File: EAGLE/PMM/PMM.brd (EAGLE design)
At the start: 76.2 x 50.8 mm, 19 parts, among them J1 TB001-500-12BE, K1 EC2-5NU, K2 G6DN-1A_DC5, K3 35701331, K4 35701331

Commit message: Minor format fixes
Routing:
- net N$5: track 75.5 -> 72.5 mm
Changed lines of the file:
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@@
 <contactref element="K2" pad="1"/>
 <wire x1="69.85" y1="17.78" x2="67.31" y2="20.32" width="0.254" layer="16"/>
-<wire x1="67.31" y1="20.32" x2="33.02" y2="20.32" width="0.254" layer="16"/>
-<wire x1="33.02" y1="20.32" x2="24.13" y2="29.21" width="0.254" layer="16"/>
-<wire x1="24.13" y1="29.21" x2="24.13" y2="34.29" width="0.254" layer="16"/>
-<wire x1="24.13" y1="34.29" x2="13.97" y2="44.45" width="0.254" layer="16"/>
+<wire x1="67.31" y1="20.32" x2="38.1" y2="20.32" width="0.254" layer="16"/>
+<wire x1="38.1" y1="20.32" x2="13.97" y2="44.45" width="0.254" layer="16"/>
 <wire x1="13.97" y1="44.45" x2="10.16" y2="44.45" width="0.254" layer="16"/>
 <wire x1="10.16" y1="44.45" x2="8.89" y2="45.72" width="0.254" layer="16"/>

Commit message: Updated C4 value
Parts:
- C4: value 0.33uF -> 0.47uF
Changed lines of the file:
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@@
 <attribute name="VALUE" x="64.008" y="41.275" size="1.27" layer="27" ratio="10"/>
 </element>
-<element name="C4" library="capacitor-wima" library_urn="urn:adsk.eagle:library:116" package="C10B6" package3d_urn="urn:adsk.eagle:package:5401/1" value="0.33uF" x="31.75" y="38.1" smashed="yes" rot="R180">
+<element name="C4" library="capacitor-wima" library_urn="urn:adsk.eagle:library:116" package="C10B6" package3d_urn="urn:adsk.eagle:package:5401/1" value="0.47uF" x="31.75" y="38.1" smashed="yes" rot="R180">
 <attribute name="NAME" x="27.94" y="34.798" size="1.27" layer="25" ratio="10" rot="R180"/>
 <attribute name="POPULARITY" value="0" x="31.75" y="38.1" size="1.778" layer="27" rot="R180" display="off"/>

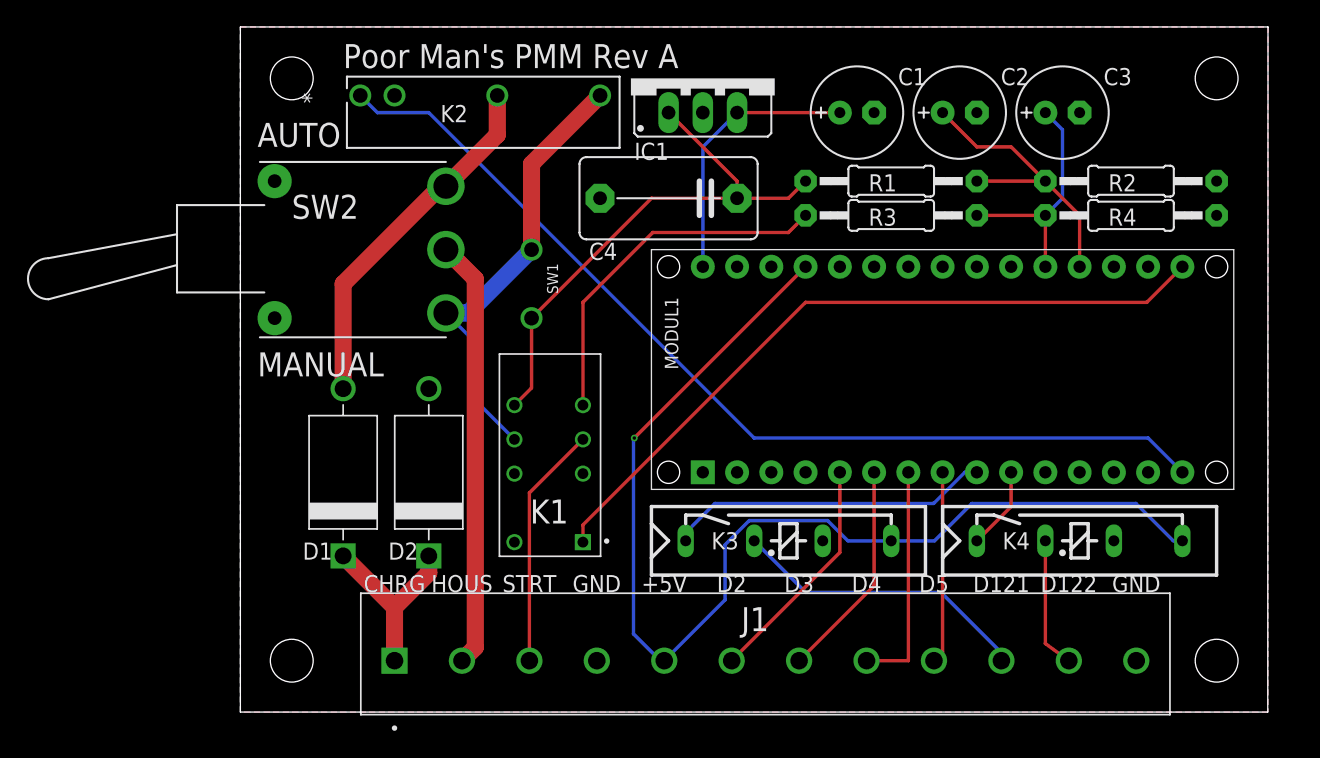
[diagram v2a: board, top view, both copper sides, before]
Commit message: Switched D12 & D13 to have on-board indicator for on state
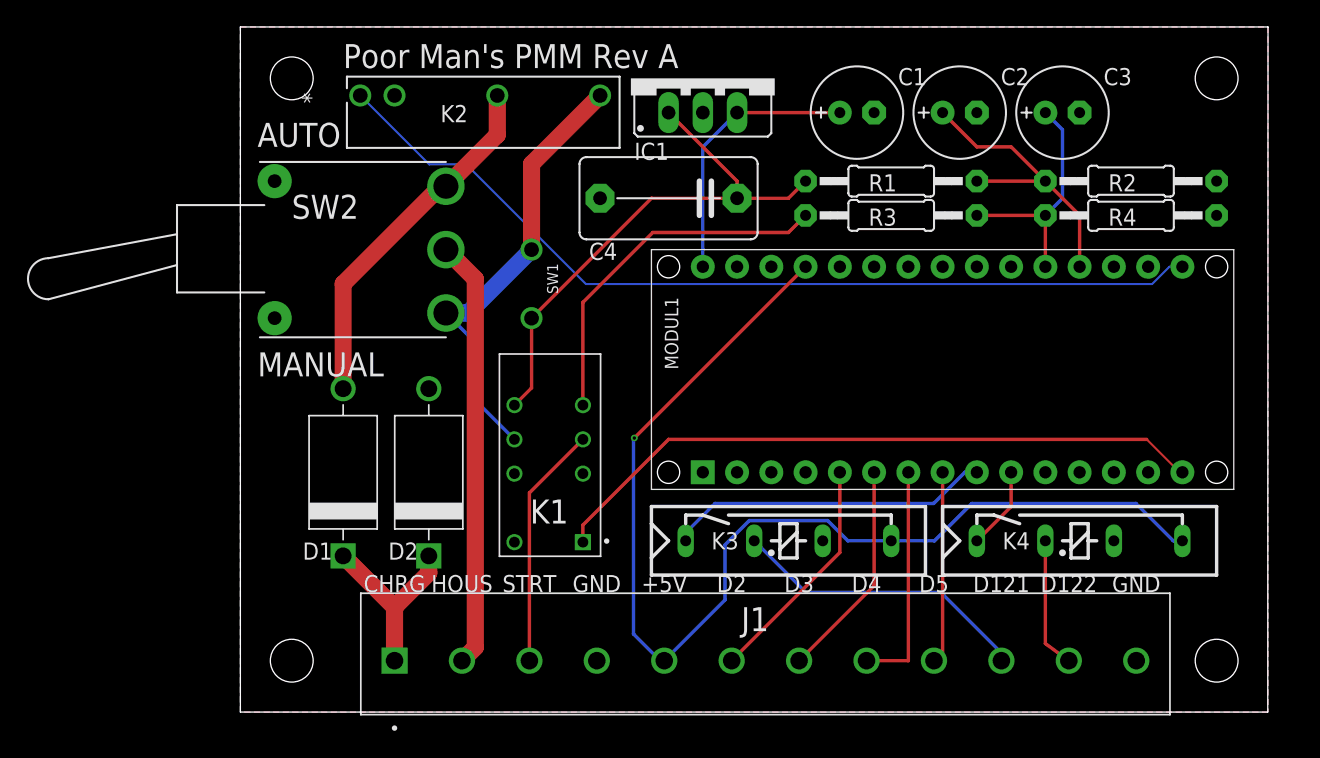
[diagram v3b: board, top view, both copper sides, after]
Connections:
- removed net N$6: K1.1, MODUL1.J2.15
- new net N$22: K1.1, MODUL1.J1.15
- net N$5: now also MODUL1.J2.15; no longer MODUL1.J1.15
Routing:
- net N$6: track 53.7 -> 0.00 mm
- net N$22: track 0.00 -> 49.4 mm
- net N$5: track 72.5 -> 67.3 mm
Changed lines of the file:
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@@
 <wire x1="30.48" y1="38.1" x2="36.83" y2="38.1" width="0.254" layer="1"/>
-</signal>
-<signal name="N$5">
-<contactref element="MODUL1" pad="J1.15"/>
-<contactref element="K2" pad="1"/>
-<wire x1="69.85" y1="17.78" x2="67.31" y2="20.32" width="0.254" layer="16"/>
-<wire x1="67.31" y1="20.32" x2="38.1" y2="20.32" width="0.254" layer="16"/>
-<wire x1="38.1" y1="20.32" x2="13.97" y2="44.45" width="0.254" layer="16"/>
-<wire x1="13.97" y1="44.45" x2="10.16" y2="44.45" width="0.254" layer="16"/>
-<wire x1="10.16" y1="44.45" x2="8.89" y2="45.72" width="0.254" layer="16"/>
-</signal>
-<signal name="N$6">
-<contactref element="MODUL1" pad="J2.15"/>
-<contactref element="K1" pad="1"/>
-<wire x1="69.85" y1="33.02" x2="67.21" y2="30.38" width="0.254" layer="1"/>
-<wire x1="67.21" y1="30.38" x2="41.91" y2="30.38" width="0.254" layer="1"/>
-<wire x1="41.91" y1="30.38" x2="25.4" y2="13.87" width="0.254" layer="1"/>
-<wire x1="25.4" y1="13.87" x2="25.4" y2="12.6" width="0.254" layer="1"/>
 </signal>
 <signal name="GND">
@@
 <wire x1="57.15" y1="15.24" x2="54.61" y2="12.7" width="0.254" layer="1"/>
 </signal>
+<signal name="N$22">
+<contactref element="MODUL1" pad="J1.15"/>
+<contactref element="K1" pad="1"/>
+<wire x1="67.21" y1="20.22" x2="31.75" y2="20.22" width="0.254" layer="1"/>
+<wire x1="31.75" y1="20.22" x2="25.4" y2="13.87" width="0.254" layer="1"/>
+<wire x1="25.4" y1="13.87" x2="25.4" y2="12.6" width="0.254" layer="1"/>
+<wire x1="69.85" y1="17.78" x2="69.65" y2="17.78" width="0.1524" layer="1"/>
+<wire x1="69.65" y1="17.78" x2="67.21" y2="20.22" width="0.1524" layer="1"/>
+</signal>
+<signal name="N$5">
+<contactref element="MODUL1" pad="J2.15"/>
+<contactref element="K2" pad="1"/>
+<wire x1="69.85" y1="33.02" x2="68.89053125" y2="33.02" width="0.1524" layer="16"/>
+<wire x1="14.00175" y1="40.60825" x2="8.89" y2="45.72" width="0.1524" layer="16"/>
+<wire x1="25.62444375" y1="31.7373" x2="16.75349375" y2="40.60825" width="0.1524" layer="16"/>
+<wire x1="16.75349375" y1="40.60825" x2="14.00175" y2="40.60825" width="0.1524" layer="16"/>
+<wire x1="68.89053125" y1="33.02" x2="67.60783125" y2="31.7373" width="0.1524" layer="16"/>
+<wire x1="67.60783125" y1="31.7373" x2="25.62444375" y2="31.7373" width="0.1524" layer="16"/>
+</signal>
 </signals>

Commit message: Corrected SW2 footprint
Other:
- board text added: "Poor Man's PMM Rev B"
- board text removed: "Poor Man's PMM Rev A"
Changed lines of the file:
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@@
 <hole x="72.39" y="46.99" drill="3.175"/>
 <hole x="72.39" y="3.81" drill="3.175"/>
-<text x="7.62" y="49.53" size="1.778" layer="21" align="top-left">Poor Man's PMM Rev A</text>
+<text x="7.62" y="49.53" size="1.778" layer="21" align="top-left">Poor Man's PMM Rev B</text>
 <text x="26.4287" y="8.89" size="1.27" layer="21" align="bottom-center">GND</text>
 <text x="21.42998125" y="8.89" size="1.27" layer="21" align="bottom-center">STRT</text>

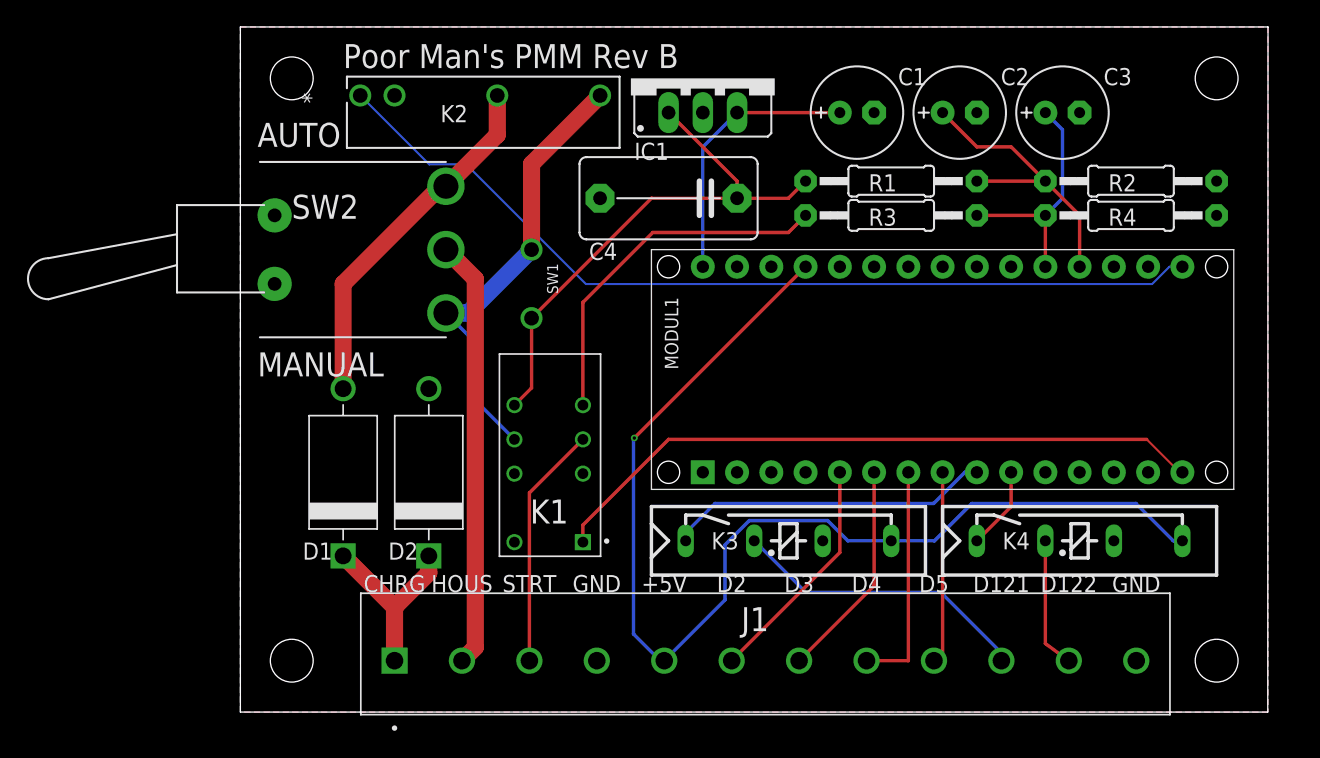
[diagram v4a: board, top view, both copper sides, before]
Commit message: Added indicator LEDs
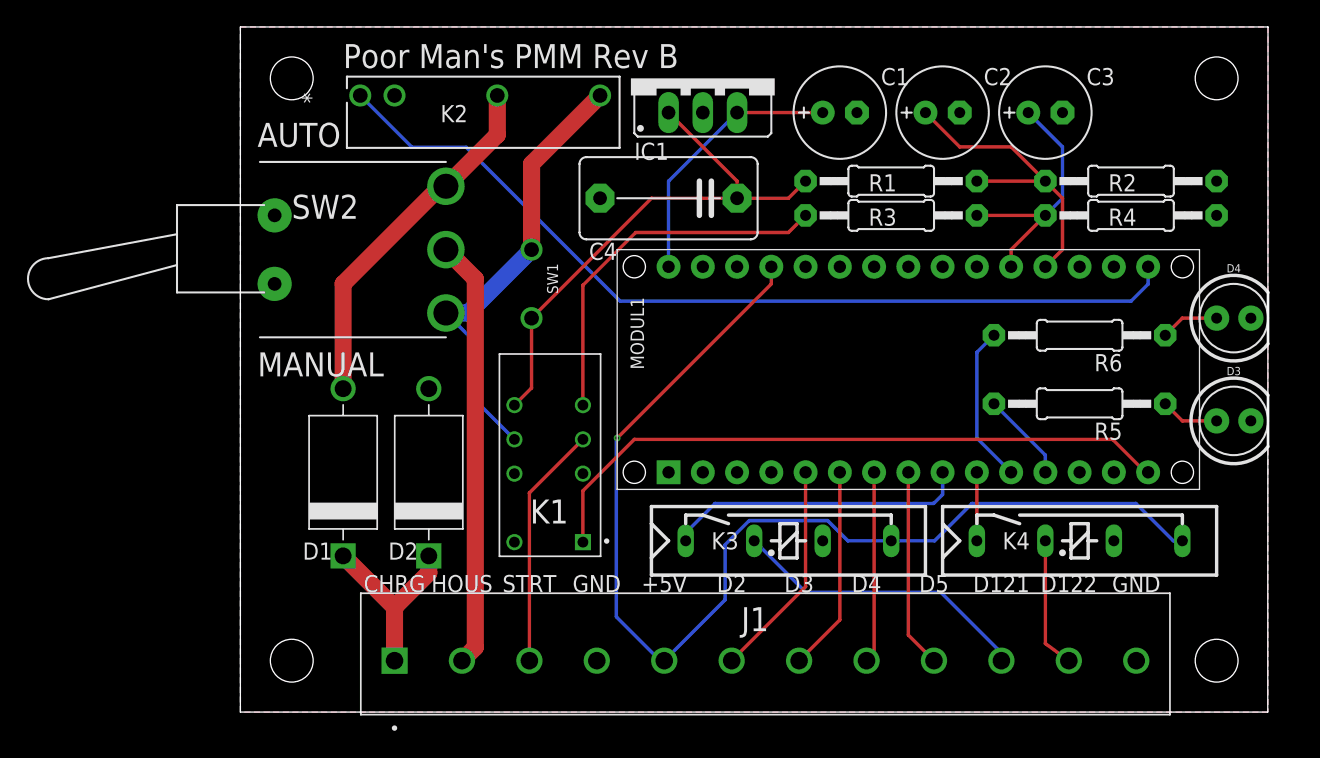
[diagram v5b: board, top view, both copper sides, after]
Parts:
- added D3: GRN, SparkFun-LED:LED_5MM-KIT
- added D4: YLW, SparkFun-LED:LED_5MM-KIT
- added R5, R6: 220, adafruit:0207/12
- moved MODUL1 2.54 mm to (49.5, 25.4)
- moved C2 1.27 mm to (52.1, 44.5)
- moved C3 1.27 mm to (59.7, 44.5)
- moved C1 1.27 mm to (44.5, 44.5)
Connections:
- new net N$23: D3.A, R5.1
- new net N$24: MODUL1.J1.11, R6.2
- new net N$25: MODUL1.J1.12, R5.2
- new net N$6: D4.A, R6.1
- net GND: now also D3.K, D4.K
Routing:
- net N$24: track 0.00 -> 11.7 mm
- net N$25: track 0.00 -> 6.66 mm
- net N$6: track 0.00 -> 4.34 mm
- net N$23: track 0.00 -> 4.34 mm
- net N$16: track 17.1 -> 14.5 mm
- net N$11: track 17.6 -> 19.1 mm
- net N$19: track 24.0 -> 22.5 mm
- net N$8: track 22.2 -> 23.5 mm
- net N$14: track 17.3 -> 16.2 mm
- net N$21: track 6.13 -> 5.08 mm
- net N$15: track 16.3 -> 15.2 mm
- net N$22: track 49.4 -> 48.3 mm
- net N$12: track 26.8 -> 27.5 mm
- net N$5: track 67.3 -> 66.5 mm
- net N$17: track 14.2 -> 14.8 mm

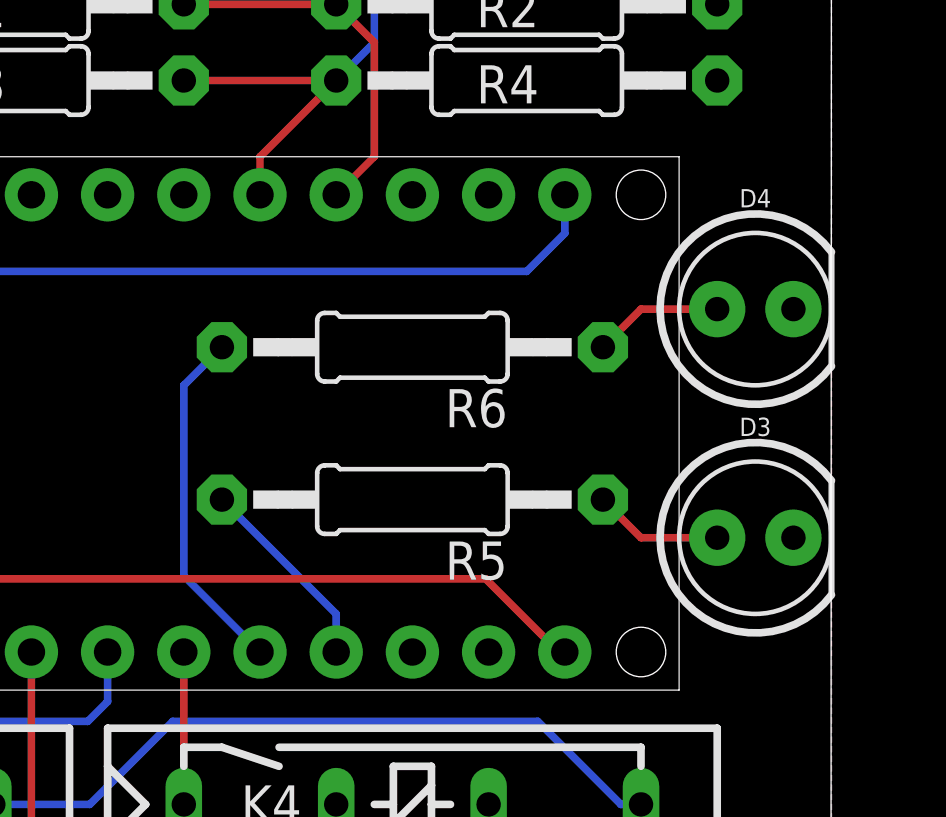
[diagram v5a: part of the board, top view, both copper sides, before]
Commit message: Rotated LEDs to bring pads in from board edge
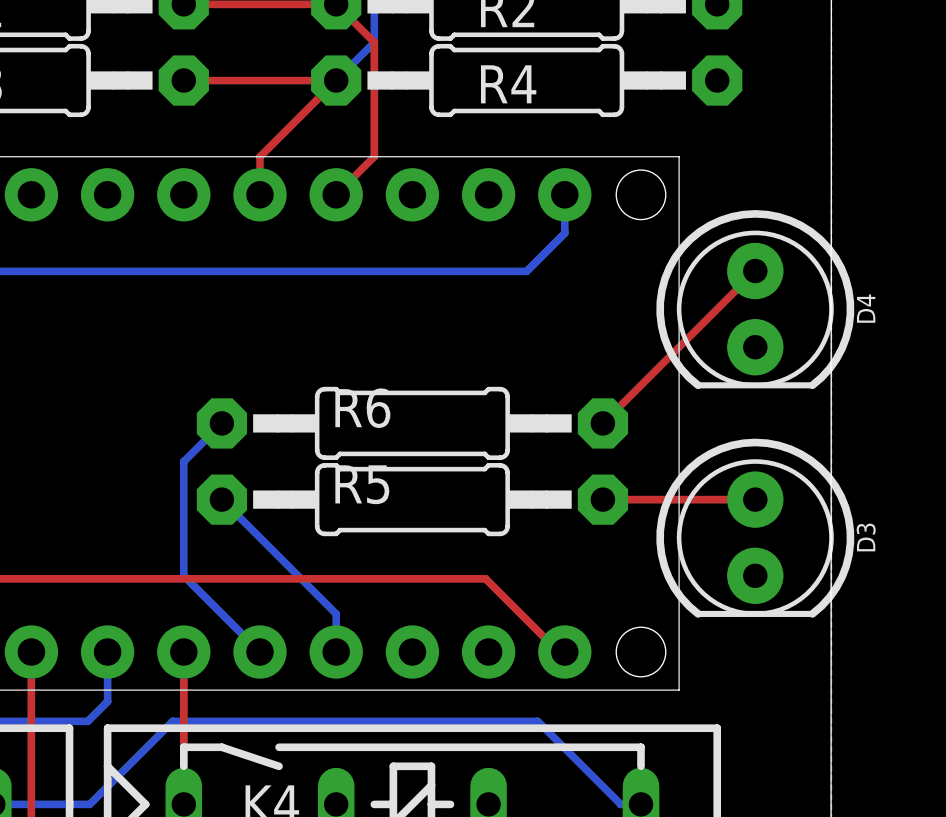
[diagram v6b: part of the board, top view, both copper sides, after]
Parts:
- moved R6 2.54 mm to (62.2, 25.4)
- turned D3 to 270 degrees
- turned D4 to 270 degrees
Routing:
- net N$6: track 4.34 -> 7.18 mm
- net N$24: track 11.7 -> 9.20 mm
- net N$23: track 4.34 -> 5.08 mm
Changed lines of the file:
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@@
 <attribute name="VALUE" x="59.69" y="15.875" size="1.27" layer="27"/>
 </element>
-<element name="D3" library="SparkFun-LED" package="LED_5MM-KIT" value="GRN" x="73.66" y="21.59" smashed="yes">
-<attribute name="NAME" x="73.66" y="24.9809" size="0.6096" layer="25" font="vector" ratio="20" align="bottom-center"/>
-<attribute name="VALUE" x="73.6854" y="18.1991" size="0.6096" layer="27" font="vector" ratio="20" align="top-center"/>
-</element>
-<element name="D4" library="SparkFun-LED" package="LED_5MM-KIT" value="YLW" x="73.66" y="29.21" smashed="yes">
-<attribute name="NAME" x="73.66" y="32.6009" size="0.6096" layer="25" font="vector" ratio="20" align="bottom-center"/>
-<attribute name="VALUE" x="73.6854" y="25.8191" size="0.6096" layer="27" font="vector" ratio="20" align="top-center"/>
+<element name="D3" library="SparkFun-LED" package="LED_5MM-KIT" value="GRN" x="73.66" y="21.59" smashed="yes" rot="R270">
+<attribute name="NAME" x="77.0509" y="21.59" size="0.6096" layer="25" font="vector" ratio="20" rot="R270" align="bottom-center"/>
+<attribute name="VALUE" x="70.2691" y="21.5646" size="0.6096" layer="27" font="vector" ratio="20" rot="R270" align="top-center"/>
+</element>
+<element name="D4" library="SparkFun-LED" package="LED_5MM-KIT" value="YLW" x="73.66" y="29.21" smashed="yes" rot="R270">
+<attribute name="NAME" x="77.0509" y="29.21" size="0.6096" layer="25" font="vector" ratio="20" rot="R270" align="bottom-center"/>
+<attribute name="VALUE" x="70.2691" y="29.1846" size="0.6096" layer="27" font="vector" ratio="20" rot="R270" align="top-center"/>
 </element>
 <element name="R5" library="adafruit" library_urn="urn:adsk.eagle:library:420" package="0207/12" package3d_urn="urn:adsk.eagle:package:6240598/1" value="220" x="62.23" y="22.86" smashed="yes" rot="R180">
-<attribute name="NAME" x="65.405" y="21.463" size="1.27" layer="25" ratio="10" rot="R180"/>
+<attribute name="NAME" x="61.595" y="24.003" size="1.27" layer="25" ratio="10" rot="R180"/>
 <attribute name="VALUE" x="64.516" y="23.5458" size="1.27" layer="27" ratio="10" rot="R180"/>
 </element>
-<element name="R6" library="adafruit" library_urn="urn:adsk.eagle:library:420" package="0207/12" package3d_urn="urn:adsk.eagle:package:6240598/1" value="220" x="62.23" y="27.94" smashed="yes" rot="R180">
-<attribute name="NAME" x="65.405" y="26.543" size="1.27" layer="25" ratio="10" rot="R180"/>
-<attribute name="VALUE" x="64.516" y="28.6258" size="1.27" layer="27" ratio="10" rot="R180"/>
+<element name="R6" library="adafruit" library_urn="urn:adsk.eagle:library:420" package="0207/12" package3d_urn="urn:adsk.eagle:package:6240598/1" value="220" x="62.23" y="25.4" smashed="yes" rot="R180">
+<attribute name="NAME" x="61.595" y="26.543" size="1.27" layer="25" ratio="10" rot="R180"/>
+<attribute name="VALUE" x="64.516" y="26.0858" size="1.27" layer="27" ratio="10" rot="R180"/>
 </element>
 </elements>
@@
 <contactref element="R6" pad="1"/>
 <contactref element="D4" pad="A"/>
-<wire x1="68.58" y1="27.94" x2="69.85" y2="29.21" width="0.254" layer="1"/>
-<wire x1="69.85" y1="29.21" x2="72.39" y2="29.21" width="0.254" layer="1"/>
+<wire x1="68.58" y1="25.4" x2="73.66" y2="30.48" width="0.254" layer="1"/>
 </signal>
 <signal name="N$23">
 <contactref element="R5" pad="1"/>
 <contactref element="D3" pad="A"/>
-<wire x1="68.58" y1="22.86" x2="69.85" y2="21.59" width="0.254" layer="1"/>
-<wire x1="69.85" y1="21.59" x2="72.39" y2="21.59" width="0.254" layer="1"/>
+<wire x1="68.58" y1="22.86" x2="73.66" y2="22.86" width="0.254" layer="1"/>
 </signal>
 <signal name="N$24">
 <contactref element="R6" pad="2"/>
 <contactref element="MODUL1" pad="J1.11"/>
-<wire x1="55.88" y1="27.94" x2="54.61" y2="26.67" width="0.254" layer="16"/>
-<wire x1="54.61" y1="26.67" x2="54.61" y2="20.32" width="0.254" layer="16"/>
+<wire x1="55.88" y1="25.4" x2="54.61" y2="24.13" width="0.254" layer="16"/>
+<wire x1="54.61" y1="24.13" x2="54.61" y2="20.32" width="0.254" layer="16"/>
 <wire x1="54.61" y1="20.32" x2="57.15" y2="17.78" width="0.254" layer="16"/>
 </signal>
@@
 <mfgpreviewcolor name="substratecolor" color="0xFF786E46"/>
 </mfgpreviewcolors>
-<errors>
-</errors>
 </board>
 </drawing>
